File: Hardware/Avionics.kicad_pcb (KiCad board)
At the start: 2 copper layers, 76 x 76 mm, 0 parts

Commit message: Added most parts to schematic and created library part for RP2040
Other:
- copper layers 2 -> 4
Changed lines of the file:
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@@
   (paper "A4")
   (layers
-    (0 "F.Cu" signal)
-    (31 "B.Cu" signal)
-    (32 "B.Adhes" user "B.Adhesive")
-    (33 "F.Adhes" user "F.Adhesive")
+    (0 "F.Cu" signal "Front")
+    (1 "In1.Cu" signal)
+    (2 "In2.Cu" signal)
+    (31 "B.Cu" signal "Back")
     (34 "B.Paste" user)
     (35 "F.Paste" user)
@@
     (38 "B.Mask" user)
     (39 "F.Mask" user)
-    (40 "Dwgs.User" user "User.Drawings")
-    (41 "Cmts.User" user "User.Comments")
-    (42 "Eco1.User" user "User.Eco1")
-    (43 "Eco2.User" user "User.Eco2")
     (44 "Edge.Cuts" user)
     (45 "Margin" user)
     (46 "B.CrtYd" user "B.Courtyard")
     (47 "F.CrtYd" user "F.Courtyard")
-    (48 "B.Fab" user)
     (49 "F.Fab" user)
-    (50 "User.1" user)
-    (51 "User.2" user)
-    (52 "User.3" user)
-    (53 "User.4" user)
-    (54 "User.5" user)
-    (55 "User.6" user)
-    (56 "User.7" user)
-    (57 "User.8" user)
-    (58 "User.9" user)
   )
   (setup
+    (stackup
+      (layer "F.SilkS" (type "Top Silk Screen"))
+      (layer "F.Paste" (type "Top Solder Paste"))
+      (layer "F.Mask" (type "Top Solder Mask") (thickness 0.01))
+      (layer "F.Cu" (type "copper") (thickness 0.035))
+      (layer "dielectric 1" (type "core") (thickness 0.48) (material "FR4") (epsilon_r 4.5) (loss_tangent 0.02))
+      (layer "In1.Cu" (type "copper") (thickness 0.035))
+      (layer "dielectric 2" (type "prepreg") (thickness 0.48) (material "FR4") (epsilon_r 4.5) (loss_tangent 0.02))
+      (layer "In2.Cu" (type "copper") (thickness 0.035))
+      (layer "dielectric 3" (type "core") (thickness 0.48) (material "FR4") (epsilon_r 4.5) (loss_tangent 0.02))
+      (layer "B.Cu" (type "copper") (thickness 0.035))
+      (layer "B.Mask" (type "Bottom Solder Mask") (thickness 0.01))
+      (layer "B.Paste" (type "Bottom Solder Paste"))
+      (layer "B.SilkS" (type "Bottom Silk Screen"))
+      (copper_finish "None")
+      (dielectric_constraints no)
+    )
     (pad_to_mask_clearance 0)
+    (solder_mask_min_width 0.1016)
     (pcbplotparams
       (layerselection 0x00010fc_ffffffff)
@@
   )
   (net 0 "")
-  (gr_circle (center 152.4 101.6) (end 190.4 101.6) (layer "Edge.Cuts") (width 0.1) (fill none))
+  (gr_circle locked (center 152.4 101.6) (end 190.4 101.6) (layer "Edge.Cuts") (width 0.1) (fill none))
 )

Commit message: Layout complete, pending review
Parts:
- added C1: 1uF, Capacitor_SMD:C_0402_1005Metric, F.Cu at (154.7, 86.6)
- added C10: 100nF, Capacitor_SMD:C_0402_1005Metric, F.Cu at (146.1, 93.3)
- added C11: 10uF, Capacitor_SMD:C_0805_2012Metric, F.Cu at (169.7, 103.1)
- added C12: 100nF, Capacitor_SMD:C_0402_1005Metric, F.Cu at (151.6, 97.5)
- added C13: 100nF, Capacitor_SMD:C_0402_1005Metric, F.Cu at (157.0, 93.1)
- added C14: 10uF, Capacitor_SMD:C_0805_2012Metric, F.Cu at (163.9, 106.9)
- added C15: 100nF, Capacitor_SMD:C_0402_1005Metric, F.Cu at (157.0, 89.5)
- added C16: 100nF, Capacitor_SMD:C_0402_1005Metric, F.Cu at (157.0, 88.3)
- added C17: 100nF, Capacitor_SMD:C_0402_1005Metric, F.Cu at (151.0, 84.6)
- added C18: 100nF, Capacitor_SMD:C_0402_1005Metric, F.Cu at (152.0, 84.6)
- added C19: 100nF, Capacitor_SMD:C_0402_1005Metric, F.Cu at (154.2, 117.3)
- added C2: 2.2uF, Capacitor_SMD:C_0603_1608Metric, F.Cu at (138.7, 80.8)
- added C20: 100uF, Capacitor_SMD:CP_Elec_8x6.5, F.Cu at (152.4, 122.6)
- added C21: 100nF, Capacitor_SMD:C_0402_1005Metric, F.Cu at (142.5, 103.7)
- added C22: 100nF, Capacitor_SMD:C_0402_1005Metric, F.Cu at (144.8, 103.0)
- added C23: 10uF, Capacitor_SMD:C_0805_2012Metric, F.Cu at (136.3, 101.1)
- added C3: 100nF, Capacitor_SMD:C_0402_1005Metric, F.Cu at (152.7, 97.4)
- added C4: 100nF, Capacitor_SMD:C_0402_1005Metric, F.Cu at (138.4, 82.2)
- added C5: 27pF, Capacitor_SMD:C_0603_1608Metric, F.Cu at (150.6, 103.1)
- added C6: 27pF, Capacitor_SMD:C_0603_1608Metric, F.Cu at (153.7, 100.4)
- added C7: 100nF, Capacitor_SMD:C_0402_1005Metric, F.Cu at (150.0, 84.6)
- added C8: 1uF, Capacitor_SMD:C_0402_1005Metric, F.Cu at (155.7, 86.6)
- added C9: 100nF, Capacitor_SMD:C_0402_1005Metric, F.Cu at (146.3, 89.4)
- added D1: MBR120, Diode_SMD:D_SOD-123F, F.Cu at (156.5, 75.2)
- added D2: PWR, LED_SMD:LED_0603_1608Metric, F.Cu at (161.2, 80.5)
- added D3: SK6812BSIDE, SK6812B:SK6812B_Side, F.Cu at (144.7, 67.3)
- added G***: LOGO, Silkscreen:Qwiic, F.Cu at (133.1, 114.3)
- added G***: LOGO, Silkscreen:WSGC, B.Cu at (147.4, 101.6)
- added G***: LOGO, Silkscreen:MSOE, B.Cu at (132.4, 101.6)
- added H1: M3, MountingHole:MountingHole_3.2mm_M3_Pad, F.Cu at (131.9, 81.1)
- added H2: M3, MountingHole:MountingHole_3.2mm_M3_Pad, F.Cu at (172.9, 81.1)
- added H3: M3, MountingHole:MountingHole_3.2mm_M3_Pad, F.Cu at (172.9, 122.1)
- added H4: M3, MountingHole:MountingHole_3.2mm_M3_Pad, F.Cu at (131.9, 122.1)
- added J1: DX07S016JA1R1500, DX07S016JA1R1500:DX07S016JA1R1500, F.Cu at (152.4, 70.7)
- added J2: SWD, Connector_PinHeader_1.27mm:PinHeader_2x05_P1.27mm_Vertical_SMD, F.Cu at (156.6, 105.9)
- added J3: LiPo 4s, XT60PW-M:AMASS_XT60PW-M, B.Cu at (169.2, 101.6)
- added J4: Qwiic, Connector_JST:JST_SH_BM04B-SRSS-TB_1x04-1MP_P1.00mm_Vertical, F.Cu at (142.4, 114.3)
- added J5: PS-562Q, Connector_JST:JST_XH_B2B-XH-A_1x02_P2.50mm_Vertical, B.Cu at (168.6, 88.6)
- added J6: DM3AT-SF-PEJM5, Connector_Card:microSD_HC_Hirose_DM3AT-SF-PEJM5, F.Cu at (125.7, 101.6)
- added J7: XD-3420, TerminalBlock_Phoenix:TerminalBlock_Phoenix_PT-1,5-2-3.5-H_1x02_P3.50mm_Horizontal, F.Cu at (161.5, 113.9)
- added Q1: BSS138, Package_TO_SOT_SMD:SOT-23, F.Cu at (161.2, 89.5)
- added R1: 10KΩ, Resistor_SMD:R_0603_1608Metric, F.Cu at (159.3, 101.2)
- added R10: 27Ω, Resistor_SMD:R_0402_1005Metric, F.Cu at (153.7, 86.6)
- added R11: 27Ω, Resistor_SMD:R_0402_1005Metric, F.Cu at (152.7, 86.6)
- added R12: 2.2KΩ, Resistor_SMD:R_0603_1608Metric, F.Cu at (142.9, 110.6)
- added R13: 2.2KΩ, Resistor_SMD:R_0603_1608Metric, F.Cu at (139.8, 110.6)
- added R14: 47KΩ, Resistor_SMD:R_0603_1608Metric, F.Cu at (161.2, 83.9)
- added R15: 10KΩ, Resistor_SMD:R_0603_1608Metric, F.Cu at (161.2, 85.7)
- added R16: 10KΩ, Resistor_SMD:R_0603_1608Metric, F.Cu at (161.2, 92.3)
- added R17: 10KΩ, Resistor_SMD:R_0603_1608Metric, F.Cu at (139.7, 101.5)
- added R18: 10KΩ, Resistor_SMD:R_0603_1608Metric, F.Cu at (145.0, 98.9)
- added R2: 5.1KΩ, Resistor_SMD:R_0603_1608Metric, F.Cu at (154.2, 74.4)
- added R3: 5.1KΩ, Resistor_SMD:R_0603_1608Metric, F.Cu at (151.2, 74.4)
- added R4: 5.6KΩ, Resistor_SMD:R_0603_1608Metric, F.Cu at (149.5, 74.4)
- added R5: 10KΩ, Resistor_SMD:R_0603_1608Metric, F.Cu at (150.2, 77.0)
- added R6: 1KΩ, Resistor_SMD:R_0603_1608Metric, F.Cu at (147.6, 100.4)
- added R7: 10KΩ, Resistor_SMD:R_0603_1608Metric, F.Cu at (136.0, 87.5)
- added R8: 1KΩ, Resistor_SMD:R_0603_1608Metric, F.Cu at (136.0, 90.7)
- added R9: 150Ω, Resistor_SMD:R_0603_1608Metric, F.Cu at (161.2, 82.2)
- added REF**: ESD-Logo_6.6x6mm_SilkScreen, Symbol:ESD-Logo_6.6x6mm_SilkScreen, F.Cu at (147.7, 106.6)
- added SW1: RESET, Button_Switch_SMD:SW_SPST_B3U-1000P, F.Cu at (158.4, 98.6)
- added SW2: BOOT, Button_Switch_SMD:SW_SPST_B3U-1000P, F.Cu at (136.4, 94.9)
- added U1: W25Q128JVS, Package_SO:SOIC-8_5.23x5.23mm_P1.27mm, F.Cu at (139.8, 87.6)
- added U2: RP2040, RP2040:RP2040-QFN-56, F.Cu at (151.7, 92.1)
- added U3: NCP1117-3.3, Package_TO_SOT_SMD:SOT-223-3_TabPin2, F.Cu at (164.8, 101.3)
- added U4: DRV8870DDA, Package_SO:Texas_HTSOP-8-1EP_3.9x4.9mm_P1.27mm_EP2.95x4.9mm_Mask2.4x3.1mm_ThermalVias, F.Cu at (152.4, 113.9)
- added U5: LSM6DSO32, Package_LGA:LGA-14_3x2.5mm_P0.5mm_LayoutBorder3x4y, F.Cu at (142.4, 101.6)
- added Y1: 12MHz, Crystal:Crystal_SMD_Abracon_ABM8G-4Pin_3.2x2.5mm, F.Cu at (150.6, 100.4)
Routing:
- net +3V3: track 0.00 -> 131.2 mm, vias 0 -> 4
- net VCC: track 0.00 -> 55.3 mm
- net /RGB_DIN: track 0.00 -> 27.3 mm, vias 0 -> 2
- net /SD_DET: track 0.00 -> 26.8 mm
- net /~{RESET}: track 0.00 -> 25.1 mm
- net GND: track 0.00 -> 24.8 mm, vias 0 -> 28
- net /SDIO_DAT3: track 0.00 -> 24.5 mm, vias 0 -> 2
- net /I2C1_SCL: track 0.00 -> 23.2 mm, vias 0 -> 2
- net /SDIO_CMD: track 0.00 -> 22.5 mm, vias 0 -> 2
- net /MOTOR_PWM1: track 0.00 -> 22.5 mm
- net /I2C1_SDA: track 0.00 -> 21.7 mm, vias 0 -> 2
- net /MOTOR_PWM2: track 0.00 -> 21.2 mm
- net Net-(R7-Pad2): track 0.00 -> 20.5 mm
- net /USB_DET: track 0.00 -> 19.4 mm, vias 0 -> 2
- net +1V1: track 0.00 -> 19.3 mm, vias 0 -> 3
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- added copper zone on F.Cu, net +3V3
- added copper zone on F.Cu, net /USB+
- added copper zone on F.Cu, net /USB-
- added copper zone on B.Cu, net GND
- added copper zone on F.Cu, net GND
- added copper zone on F.Cu, net Net-(J7-Pad1)
- added copper zone on F.Cu, net Net-(J7-Pad2)
- added copper zone on F.Cu, net VBUS
- added copper zone on F.Cu, net VCC
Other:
- board size 76 x 76 mm -> 73 x 73 mm
- rule pad_to_mask_clearance: 0 -> 0.0508
- board text added: "- +"

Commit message: Fixed part libraries
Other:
- copper layers 4 -> 2
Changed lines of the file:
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@@
 (kicad_pcb (version 20211014) (generator pcbnew)
   (general
-    (thickness 1.6)
+    (thickness 0.57)
   )
   (paper "A4")
   (layers
     (0 "F.Cu" signal "Front")
-    (1 "In1.Cu" signal)
-    (2 "In2.Cu" signal)
     (31 "B.Cu" signal "Back")
     (34 "B.Paste" user)
@@
       (layer "F.Cu" (type "copper") (thickness 0.035))
       (layer "dielectric 1" (type "core") (thickness 0.48) (material "FR4") (epsilon_r 4.5) (loss_tangent 0.02))
-      (layer "In1.Cu" (type "copper") (thickness 0.035))
-      (layer "dielectric 2" (type "prepreg") (thickness 0.48) (material "FR4") (epsilon_r 4.5) (loss_tangent 0.02))
-      (layer "In2.Cu" (type "copper") (thickness 0.035))
-      (layer "dielectric 3" (type "core") (thickness 0.48) (material "FR4") (epsilon_r 4.5) (loss_tangent 0.02))
       (layer "B.Cu" (type "copper") (thickness 0.035))
       (layer "B.Mask" (type "Bottom Solder Mask") (thickness 0.01))
@@
     (grid_origin 152.4 101.6)
     (pcbplotparams
-      (layerselection 0x00010fc_ffffffff)
+      (layerselection 0x000f0fc_fffffff9)
       (disableapertmacros false)
       (usegerberextensions false)
@@
       (svguseinch false)
       (svgprecision 6)
-      (excludeedgelayer true)
+      (excludeedgelayer false)
       (plotframeref false)
       (viasonmask false)
@@
       (outputformat 1)
       (mirror false)
-      (drillshape 1)
+      (drillshape 0)
       (scaleselection 1)
-      (outputdirectory "")
+      (outputdirectory "C:/Users/nettesheimcj/Downloads/New folder (2)/")
     )
   )
@@
     (pad "4" smd roundrect locked (at 1.5 1.325 180) (size 0.6 1.55) (layers "F.Cu" "F.Paste" "F.Mask") (roundrect_rratio 0.25)
       (net 29 "/I2C1_SCL") (pinfunction "Pin_4") (pintype "passive"))
-    (pad "MP" smd roundrect locked (at 2.8 -1.2 180) (size 1.2 1.8) (layers "F.Cu" "F.Paste" "F.Mask") (roundrect_rratio 0.208333))
-    (pad "MP" smd roundrect locked (at -2.8 -1.2 180) (size 1.2 1.8) (layers "F.Cu" "F.Paste" "F.Mask") (roundrect_rratio 0.208333))
+    (pad "MP" smd roundrect locked (at 2.8 -1.2 180) (size 1.2 1.8) (layers "F.Cu" "F.Paste" "F.Mask") (roundrect_rratio 0.2083333333))
+    (pad "MP" smd roundrect locked (at -2.8 -1.2 180) (size 1.2 1.8) (layers "F.Cu" "F.Paste" "F.Mask") (roundrect_rratio 0.2083333333))
     (model "${KICAD6_3DMODEL_DIR}/Connector_JST.3dshapes/JST_SH_BM04B-SRSS-TB_1x04-1MP_P1.00mm_Vertical.wrl" hide
       (offset (xyz 0 0 0))
@@
     (fp_line (start 3.5 -3.5) (end 3.5 3.5) (layer "F.Fab") (width 0.1))
     (fp_line (start -2.5 -3.5) (end 3.5 -3.5) (layer "F.Fab") (width 0.1))
-    (pad "" smd roundrect (at 0.6375 -0.6375) (size 1.084435 1.084435) (layers "F.Paste") (roundrect_rratio 0.230535))
-    (pad "" smd roundrect (at 0.6375 0.6375) (size 1.084435 1.084435) (layers "F.Paste") (roundrect_rratio 0.230535))
-    (pad "" smd roundrect (at -0.6375 -0.6375) (size 1.084435 1.084435) (layers "F.Paste") (roundrect_rratio 0.230535))
-    (pad "" smd roundrect (at -0.6375 0.6375) (size 1.084435 1.084435) (layers "F.Paste") (roundrect_rratio 0.230535))
+    (pad "" smd roundrect (at 0.6375 -0.6375) (size 1.084435 1.084435) (layers "F.Paste") (roundrect_rratio 0.2305347946))
+    (pad "" smd roundrect (at 0.6375 0.6375) (size 1.084435 1.084435) (layers "F.Paste") (roundrect_rratio 0.2305347946))
+    (pad "" smd roundrect (at -0.6375 -0.6375) (size 1.084435 1.084435) (layers "F.Paste") (roundrect_rratio 0.2305347946))
+    (pad "" smd roundrect (at -0.6375 0.6375) (size 1.084435 1.084435) (layers "F.Paste") (roundrect_rratio 0.2305347946))
     (pad "1" smd roundrect (at -3.4375 -2.6) (size 0.875 0.2) (layers "F.Cu" "F.Paste" "F.Mask") (roundrect_rratio 0.25)
       (net 3 "+3V3") (pinfunction "IOVDD") (pintype "power_in"))
@@
     (fp_line (start 4.95 2.35) (end -2.45 2.35) (layer "B.Fab") (width 0.1))
     (fp_line (start -0.625 2.35) (end 0 1.35) (layer "B.Fab") (width 0.1))
-    (pad "1" thru_hole roundrect locked (at 0 0 180) (size 1.7 2) (drill 1) (layers *.Cu *.Mask) (roundrect_rratio 0.147059)
+    (pad "1" thru_hole roundrect locked (at 0 0 180) (size 1.7 2) (drill 1) (layers *.Cu *.Mask) (roundrect_rratio 0.1470588235)
       (net 4 "VCC") (pinfunction "-") (pintype "passive"))
     (pad "2" thru_hole oval locked (at 2.5 0 180) (size 1.7 2) (drill 1) (layers *.Cu *.Mask)

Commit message: Modified layout
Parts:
- removed REF**: ESD-Logo_6.6x6mm_SilkScreen, Symbol:ESD-Logo_6.6x6mm_SilkScreen
- SW1: value RESET -> ~{RESET}
- SW2: value BOOT -> ~{BOOT}
- moved J4 6.35 mm to (142.2, 108.0), turned to 0 degrees
- moved R13 4.58 mm to (144.1, 112.1), turned to 90 degrees
- moved G*** 3.24 mm to (135.3, 111.9)
- moved R17 2.52 mm to (140.8, 99.2), turned to 0 degrees
- moved R12 1.59 mm to (142.5, 112.1), turned to 90 degrees
- moved R18 1.20 mm to (143.9, 99.2), turned to 180 degrees
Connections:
- J4 pad 3: /I2C1_SDA -> /I2C0_SDA
- J4 pad 4: /I2C1_SCL -> /I2C0_SCL
- R12 pad 2: /I2C1_SDA -> /I2C0_SDA
- R13 pad 2: /I2C1_SCL -> /I2C0_SCL
- R17 pad 2: /I2C0_SDA -> /I2C1_SDA
- R18 pad 2: /I2C0_SCL -> /I2C1_SCL
- U5 pad 13: /I2C0_SCL -> /I2C1_SCL
- U5 pad 14: /I2C0_SDA -> /I2C1_SDA
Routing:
- net +3V3: track 131.2 -> 114.2 mm
- net /I2C1_SCL: track 23.2 -> 9.46 mm, vias 2 -> 0
- net /I2C1_SDA: track 21.7 -> 10.6 mm, vias 2 -> 0
- net /I2C0_SCL: track 9.81 -> 18.8 mm
- net /I2C0_SDA: track 12.6 -> 18.8 mm
- net GND: track 24.8 -> 26.5 mm, vias 28 -> 68
- net /IMU_INT: track 14.1 -> 13.6 mm, vias 2 -> 0
- added copper zone on B.Cu, net +3V3
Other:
- outline, holes or cut-outs redrawn

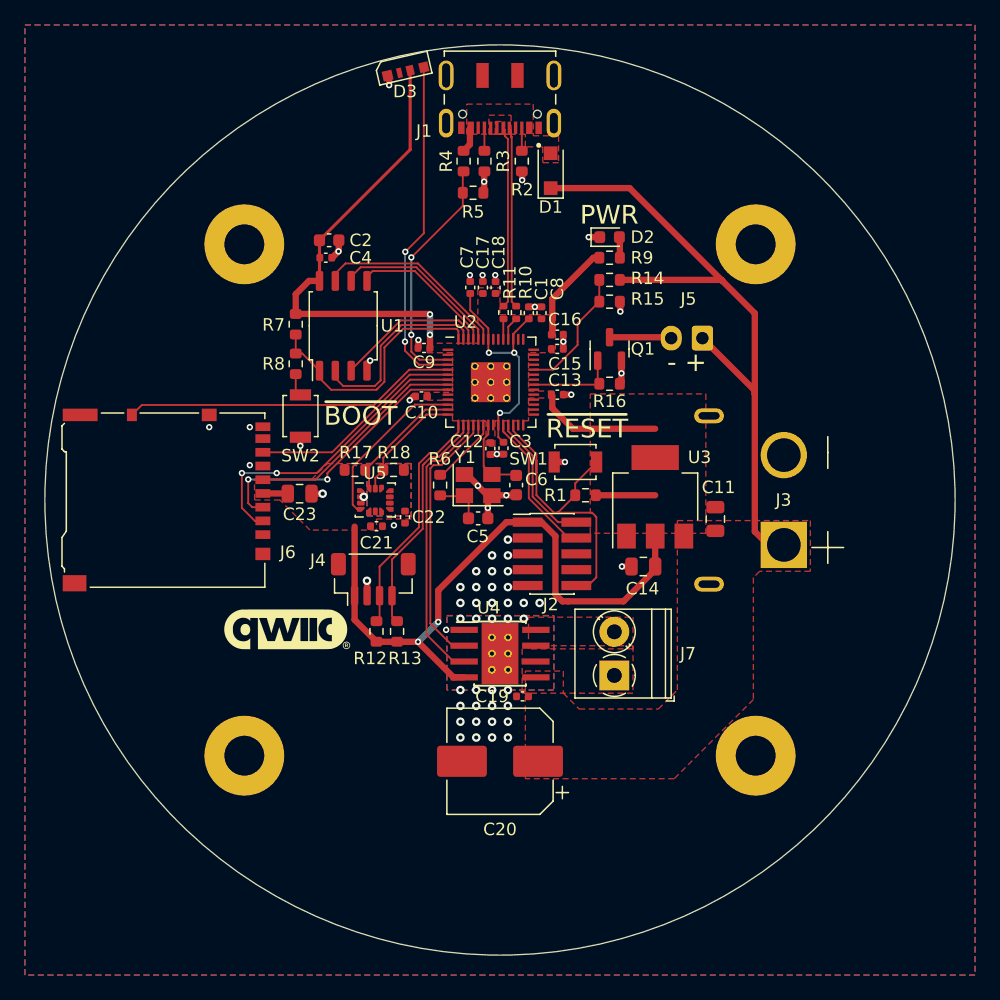
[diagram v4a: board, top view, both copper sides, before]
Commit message: Moved reference designators to fab layer
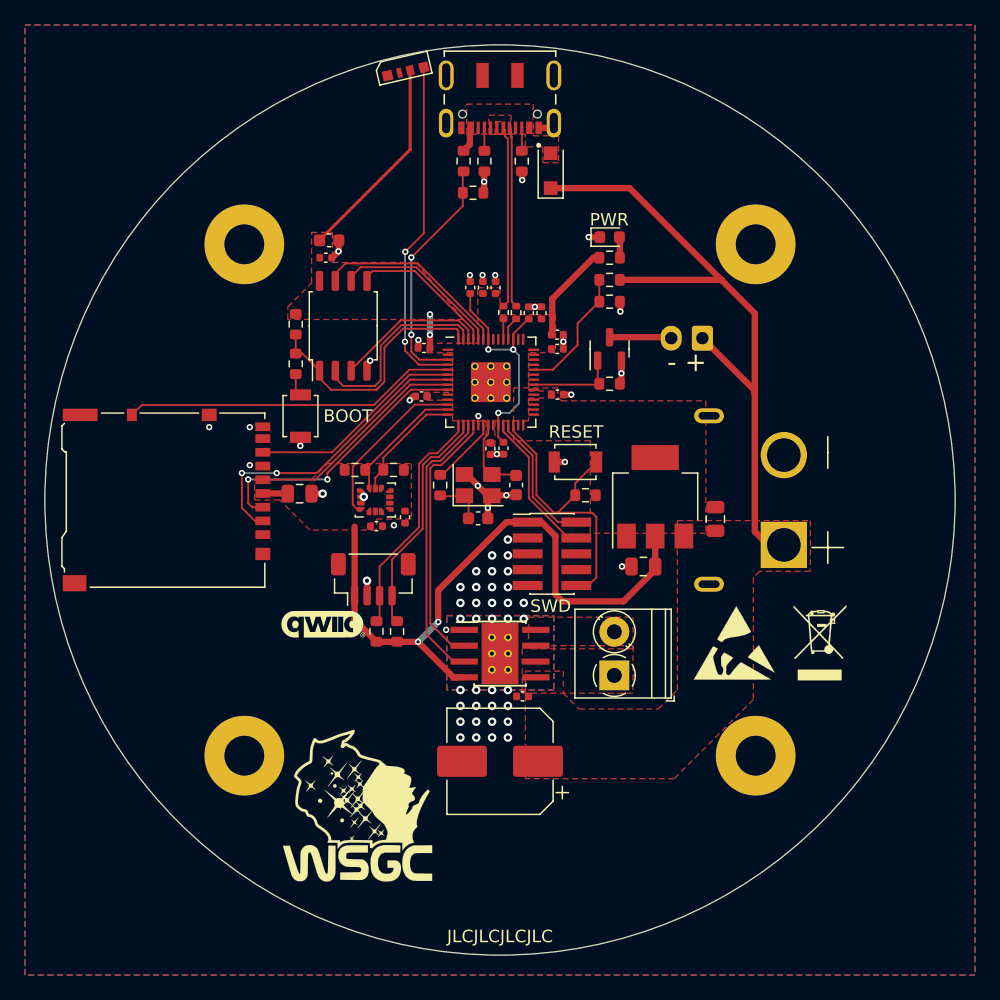
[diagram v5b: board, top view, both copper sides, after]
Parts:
- removed the G*** at (132.4, 101.6)
- added REF**: ESD-Logo_6.6x6mm_SilkScreen, Symbol:ESD-Logo_6.6x6mm_SilkScreen, F.Cu at (171.2, 113.0)
- added REF**: WEEE-Logo_4.2x6mm_SilkScreen, Symbol:WEEE-Logo_4.2x6mm_SilkScreen, F.Cu at (178.1, 113.0)
- G***: moved to F.Cu
- SW1: value ~{RESET} -> RESET
- SW2: value ~{BOOT} -> BOOT
- moved G*** 25.3 mm to (141.0, 126.1), turned to 0 degrees
- moved G*** 2.95 mm to (138.2, 111.5)
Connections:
- U2 pad 35: unconnected-(U2-Pad35) -> /SIREN
- U2 pad 37: /SIREN -> unconnected-(U2-Pad37)
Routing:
- net +3V3: track 114.2 -> 81.2 mm
- net /~{RESET}: track 25.1 -> 24.0 mm
- net GND: track 26.5 -> 27.2 mm, vias 68 -> 67
- removed copper zone on B.Cu, net +3V3
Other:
- board text added: "JLCJLCJLCJLC"
- board text added: "Mounting Ring Diameter"

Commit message: Added silkscreen logos and improved power routing
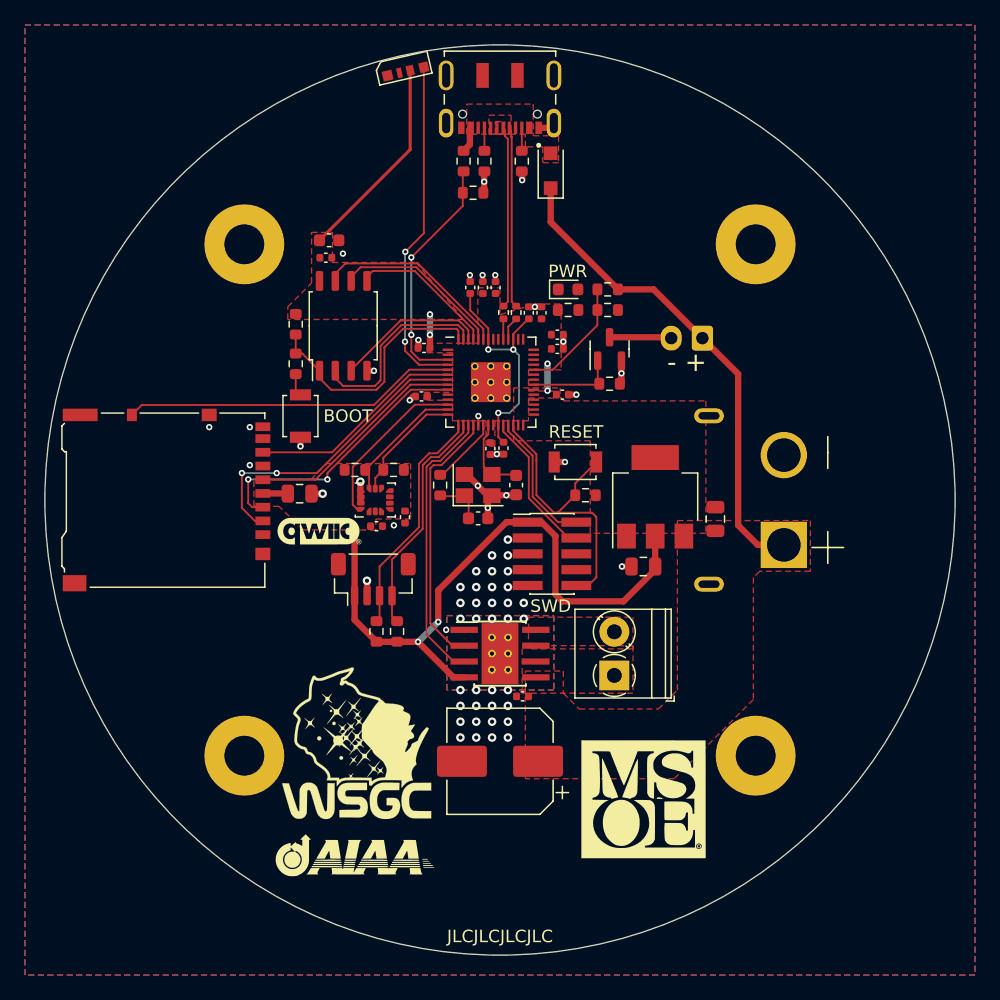
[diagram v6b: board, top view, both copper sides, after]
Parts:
- removed REF**: ESD-Logo_6.6x6mm_SilkScreen, Symbol:ESD-Logo_6.6x6mm_SilkScreen
- removed REF**: WEEE-Logo_4.2x6mm_SilkScreen, Symbol:WEEE-Logo_4.2x6mm_SilkScreen
- added G***: LOGO, Silkscreen:AIAA, F.Cu at (140.9, 130.1)
- added G***: LOGO, Silkscreen:MSOE, F.Cu at (163.9, 125.6)
- moved G*** 7.47 mm to (137.9, 104.0)
- moved D2 5.35 mm to (157.9, 84.7)
- moved R9 5.35 mm to (157.9, 86.4)
- moved G*** 5.01 mm to (140.9, 121.1)
- moved R14 0.78 mm to (161.0, 84.7)
- moved R15 0.68 mm to (161.0, 86.4)
- moved C13 0.41 mm to (157.4, 93.1)
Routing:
- net VCC: track 55.3 -> 39.3 mm
- net +3V3: track 81.2 -> 75.2 mm, vias 4 -> 6
- net GND: track 27.2 -> 25.1 mm, vias 67 -> 65
- net Net-(D2-Pad2): track 1.67 -> 0.00 mm
- net /BATT_ADC: track 10.3 -> 9.46 mm

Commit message: Final layout
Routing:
- net Net-(D2-Pad2): track 0.00 -> 1.67 mm
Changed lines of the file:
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@@
   (segment (start 149.987 73.089) (end 149.987 71.771589) (width 0.508) (layer "F.Cu") (net 7))
   (segment (start 149.479 73.597) (end 149.987 73.089) (width 0.508) (layer "F.Cu") (net 7))
+  (segment (start 158.686 86.36) (end 158.686 84.7465) (width 0.1524) (layer "F.Cu") (net 8))
+  (segment (start 158.686 84.7465) (end 158.6485 84.709) (width 0.1524) (layer "F.Cu") (net 8))
   (segment (start 146.291495 80.208353) (end 146.291495 66.892521) (width 0.1524) (layer "F.Cu") (net 9))
   (segment (start 144.78 88.9) (end 144.78 89.624973) (width 0.1524) (layer "F.Cu") (net 9))
